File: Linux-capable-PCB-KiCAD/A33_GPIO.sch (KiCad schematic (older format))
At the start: 44 parts, among them J1 UART_CONN, J2 GPIO_CONN, J3 USB_A, J4 USB_A, J5 Micro_SD_Card_Det, J6 MIC_DIFF_IN, Q1 Q_PMOS_GSD, Q2 BC547, U1 A33, U2 MMA8425Q_Gsensor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

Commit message: Added an antenna
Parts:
- AE1: footprint (none) -> Small2_4GHz_PCB_Antenna:Small2_4GHz_PCB_Antenna
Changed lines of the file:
@@
 F 0 "AE1" H 6455 5314 50  0000 L CNN
 F 1 "Antenna_Dipole" H 6455 5223 50  0000 L CNN
-F 2 "" H 6225 5400 50  0001 C CNN
+F 2 "Small2_4GHz_PCB_Antenna:Small2_4GHz_PCB_Antenna" H 6225 5400 50  0001 C CNN
 F 3 "" H 6225 5400 50  0001 C CNN
 	1    6225 5400

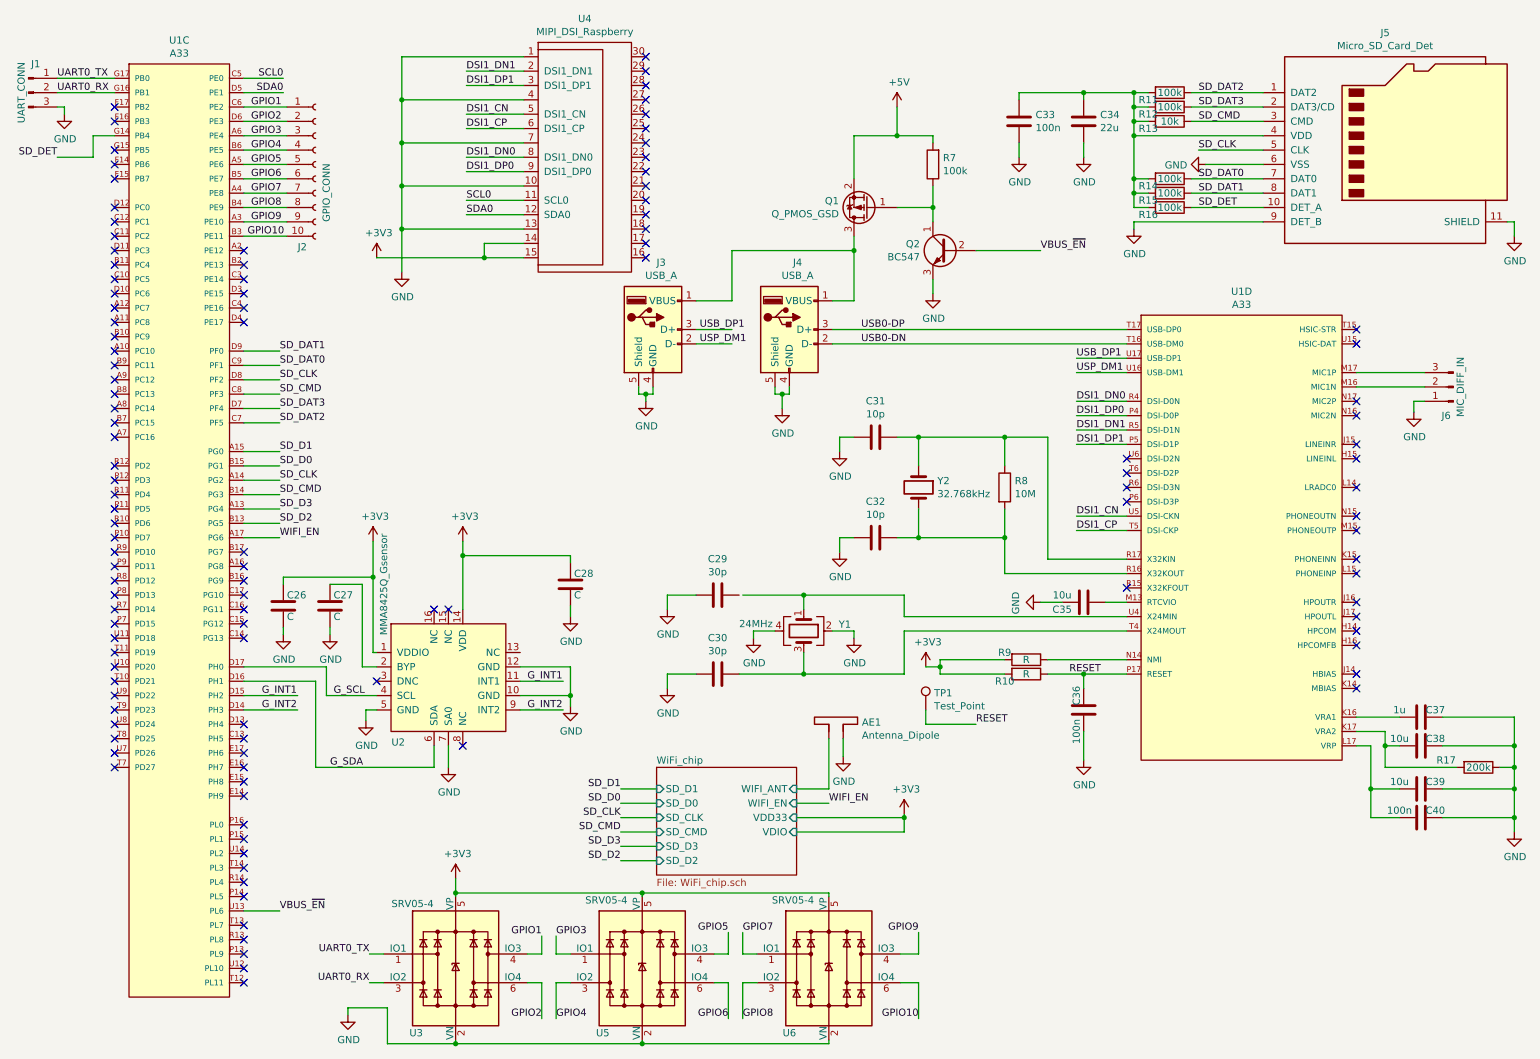
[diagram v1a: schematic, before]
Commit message: Dodao 3.3V na SD karticu, treba zamjeniti SD konektor, zavrsio napjanje, treba izracunati vrijednosti otpornika i footprint preci za komponente
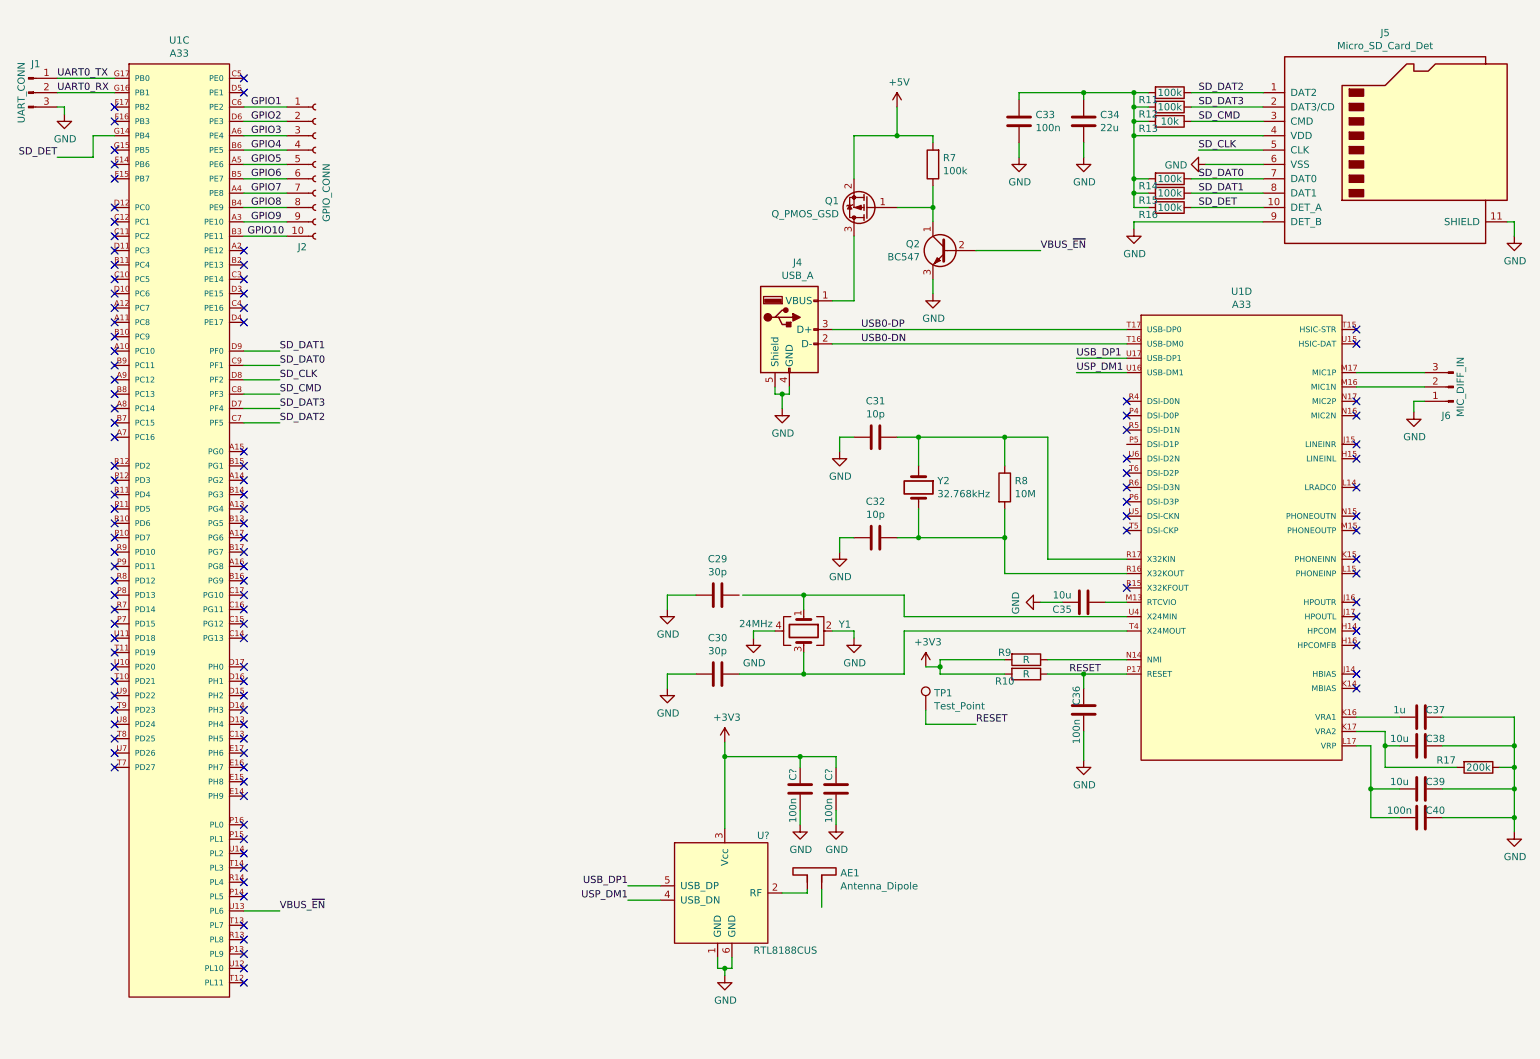
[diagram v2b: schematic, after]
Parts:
- removed C26, C27, C28: C, Capacitor_SMD:C_0603_1608Metric, symbol Linux-capable-PCB-KiCAD-rescue:C-Device
- removed J3: USB_A, Connector_USB:USB_Micro-B_Molex-105017-0001, symbol Linux-capable-PCB-KiCAD-rescue:USB_A-Connector
- removed U2: MMA8425Q_Gsensor, Package_DFN_QFN:QFN-16-1EP_3x3mm_P0.5mm_EP1.9x1.9mm, symbol MMA8425Q_Gsensor:MMA8425Q_Gsensor
- removed U3, U5, U6: SRV05-4, Package_TO_SOT_SMD:SOT-23-6, symbol Linux-capable-PCB-KiCAD-rescue:SRV05-4-Power_Protection
- removed U4: MIPI_DSI_Raspberry, Connector_FFC-FPC:Molex_502244-1530_1x15-1MP_P0.5mm_Horizontal, symbol MIPI_DSI_Raspberry:MIPI_DSI_Raspberry
- added C? (x2): 100n, Capacitor_SMD:C_0603_1608Metric, symbol Linux-capable-PCB-KiCAD-rescue:C-device
- added U?: RTL8188CUS, realtek:RTL8188CUS, symbol realtek:RTL8188CUS
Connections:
- net +3V3: now also C?.1, C?.1, U?.3 (Vcc)
- net GND: now also C?.2, C?.2, U?.1 (GND), U?.6 (GND); no longer AE1.2
- net SD_CLK: no longer U1.A14 (PG2)
- net SD_CMD: no longer U1.B14 (PG3)
- net USB_DP1: now also U?.5 (USB_DP)
- net USP_DM1: now also U?.4 (USB_DN)
- net DSI1_CN: no longer names the net of U1.U5 (DSI-CKN)
- net DSI1_CP: no longer names the net of U1.T5 (DSI-CKP)
- net DSI1_DN0: no longer names the net of U1.R4 (DSI-D0N)
- net DSI1_DN1: no longer names the net of U1.R5 (DSI-D1N)
- net DSI1_DP0: no longer names the net of U1.P4 (DSI-D0P)
- net DSI1_DP1: no longer names the net of U1.P5 (DSI-D1P)
- net G_INT1: no longer names the net of U1.D15 (PH2)
- net G_INT2: no longer names the net of U1.D14 (PH3)
- net G_SCL: no longer names the net of U1.D17 (PH0)
- net G_SDA: no longer names the net of U1.D16 (PH1)
- net SCL0: no longer names the net of U1.C5 (PE0)
- net SDA0: no longer names the net of U1.D5 (PE1)
- net SD_D0: no longer names the net of U1.B15 (PG1)
- net SD_D1: no longer names the net of U1.A15 (PG0)
- net SD_D2: no longer names the net of U1.B13 (PG5)
- net SD_D3: no longer names the net of U1.A13 (PG4)
- net WIFI_EN: no longer names the net of U1.A17 (PG6)
- net WiFi_chip/WIFI_ANT: no longer names the net of AE1.1
- net WiFi_chip/WIFI_ANT: now also U?.2 (RF)
- no-connect marks 115 -> 114
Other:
- moved on the sheet: AE1
